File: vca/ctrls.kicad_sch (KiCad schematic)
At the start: 6 parts, among them U1 LM324, U2 LM324, U3 LM324

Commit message: some fixes, starting to work on PCB
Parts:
- gave numbers to parts that had none: 3
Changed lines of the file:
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@@
   (symbol (lib_id "eurorack:C-100nF-0805") (at 193.675 40.005 0) (unit 1)
     (in_bom yes) (on_board yes)
-    (property "Reference" "C?" (id 0) (at 187.325 41.275 90)
+    (property "Reference" "C14" (id 0) (at 187.325 41.275 90)
       (effects (font (size 1.27 1.27)) (justify left))
     )
@@
   (symbol (lib_id "power:GND") (at 154.94 50.165 0) (unit 1)
     (in_bom yes) (on_board yes) (fields_autoplaced)
-    (property "Reference" "#PWR?" (id 0) (at 154.94 56.515 0)
+    (property "Reference" "#PWR0133" (id 0) (at 154.94 56.515 0)
       (effects (font (size 1.27 1.27)) hide)
     )
@@
   (symbol (lib_id "eurorack:C-100nF-0805") (at 183.515 40.005 0) (unit 1)
     (in_bom yes) (on_board yes)
-    (property "Reference" "C?" (id 0) (at 177.165 41.275 90)
+    (property "Reference" "C13" (id 0) (at 177.165 41.275 90)
       (effects (font (size 1.27 1.27)) (justify left))
     )
@@
   (symbol (lib_id "power:+5V") (at 154.94 29.845 0) (unit 1)
     (in_bom yes) (on_board yes) (fields_autoplaced)
-    (property "Reference" "#PWR?" (id 0) (at 154.94 33.655 0)
+    (property "Reference" "#PWR0134" (id 0) (at 154.94 33.655 0)
       (effects (font (size 1.27 1.27)) hide)
     )
@@
   (symbol (lib_id "power:GND") (at 144.78 76.2 0) (unit 1)
     (in_bom yes) (on_board yes) (fields_autoplaced)
-    (property "Reference" "#PWR?" (id 0) (at 144.78 82.55 0)
+    (property "Reference" "#PWR0132" (id 0) (at 144.78 82.55 0)
       (effects (font (size 1.27 1.27)) hide)
     )
@@
   (symbol (lib_id "power:GND") (at 168.91 76.2 0) (unit 1)
     (in_bom yes) (on_board yes) (fields_autoplaced)
-    (property "Reference" "#PWR?" (id 0) (at 168.91 82.55 0)
+    (property "Reference" "#PWR0131" (id 0) (at 168.91 82.55 0)
       (effects (font (size 1.27 1.27)) hide)
     )
@@
   (symbol (lib_id "eurorack:C-100nF-0805") (at 173.355 40.005 0) (unit 1)
     (in_bom yes) (on_board yes)
-    (property "Reference" "C?" (id 0) (at 167.005 41.275 90)
+    (property "Reference" "C12" (id 0) (at 167.005 41.275 90)
       (effects (font (size 1.27 1.27)) (justify left))
     )

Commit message: working on the PCB
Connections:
- net +5V renamed +5C
- net GND renamed GND2

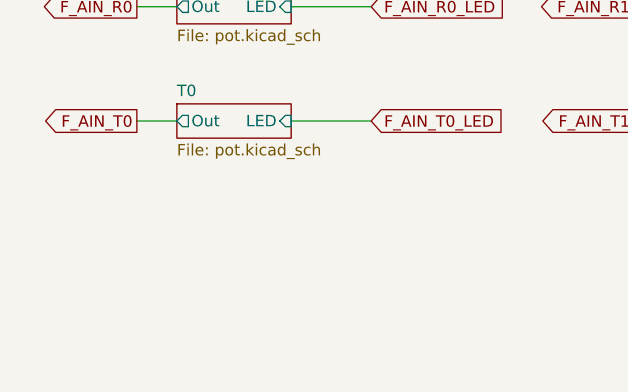
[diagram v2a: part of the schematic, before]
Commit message: Added buttons, refactored front panel, refactored power part, wip
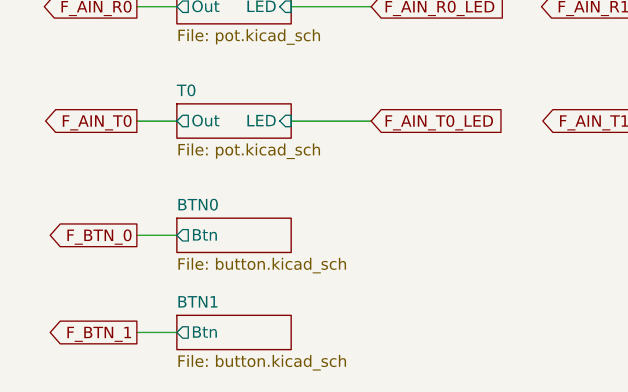
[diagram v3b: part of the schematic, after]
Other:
- added sheet BTN0 (button.kicad_sch)
- added sheet BTN1 (button.kicad_sch)
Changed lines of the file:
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@@
+    (stroke (width 0) (type default) (color 0 0 0 0))
+  )
+  (wire (pts (xy 29.21 80.645) (xy 33.655 80.645))
     (stroke (width 0) (type default) (color 0 0 0 0))
   )
@@
     (stroke (width 0) (type default) (color 0 0 0 0))
   )
+  (wire (pts (xy 29.21 91.44) (xy 33.655 91.44))
+    (stroke (width 0) (type default) (color 0 0 0 0))
+  )
   (wire (pts (xy 144.78 72.39) (xy 144.78 76.2))
     (stroke (width 0) (type default) (color 0 0 0 0))
@@
     )
   )
+  (global_label "F_BTN_1" (shape output) (at 29.21 91.44 180) (fields_autoplaced)
+    (effects (font (size 1.27 1.27)) (justify right))
+    (property "Intersheet References" "${INTERSHEET_REFS}" (id 0) (at 18.9955 91.3606 0)
+      (effects (font (size 1.27 1.27)) (justify right) hide)
+    )
+  )
   (global_label "F_AIN_S1_LED" (shape input) (at 110.49 44.45 0) (fields_autoplaced)
     (effects (font (size 1.27 1.27)) (justify left))
@@
     (property "Intersheet References" "${INTERSHEET_REFS}" (id 0) (at 125.5426 67.8656 0)
       (effects (font (size 1.27 1.27)) (justify left) hide)
+    )
+  )
+  (global_label "F_BTN_0" (shape output) (at 29.21 80.645 180) (fields_autoplaced)
+    (effects (font (size 1.27 1.27)) (justify right))
+    (property "Intersheet References" "${INTERSHEET_REFS}" (id 0) (at 18.9955 80.5656 0)
+      (effects (font (size 1.27 1.27)) (justify right) hide)
     )
   )
@@
     )
   )
+  (sheet (at 33.655 89.535) (size 12.7 3.81) (fields_autoplaced)
+    (stroke (width 0.1524) (type solid) (color 0 0 0 0))
+    (fill (color 0 0 0 0.0000))
+    (property "Sheet name" "BTN1" (id 0) (at 33.655 88.8234 0)
+      (effects (font (size 1.27 1.27)) (justify left bottom))
+    )
+    (property "Sheet file" "button.kicad_sch" (id 1) (at 33.655 93.9296 0)
+      (effects (font (size 1.27 1.27)) (justify left top))
+    )
+    (pin "Btn" output (at 33.655 91.44 180)
+      (effects (font (size 1.27 1.27)) (justify left))
+    )
+  )
   (sheet (at 33.655 42.545) (size 12.7 3.81) (fields_autoplaced)
     (stroke (width 0.1524) (type solid) (color 0 0 0 0))
@@
       (effects (font (size 1.27 1.27)) (justify left))
     )
+  )
+  (sheet (at 33.655 78.74) (size 12.7 3.81) (fields_autoplaced)
+    (stroke (width 0.1524) (type solid) (color 0 0 0 0))
+    (fill (color 0 0 0 0.0000))
+    (property "Sheet name" "BTN0" (id 0) (at 33.655 78.0284 0)
+      (effects (font (size 1.27 1.27)) (justify left bottom))
+    )
+    (property "Sheet file" "button.kicad_sch" (id 1) (at 33.655 83.1346 0)
+      (effects (font (size 1.27 1.27)) (justify left top))
+    )
+    (pin "Btn" output (at 33.655 80.645 180)
+      (effects (font (size 1.27 1.27)) (justify left))
+    )
